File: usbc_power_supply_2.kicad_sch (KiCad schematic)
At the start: 22 parts, among them J1 USB4125-GF-A-0190, J2 B2B-PH-K-SLFSN, J3 B2B-PH-K-SLFSN, Q1 DMG3415UFY4Q-7, U1 MBR0540T3G, U2 MCP73833-AMI/MF

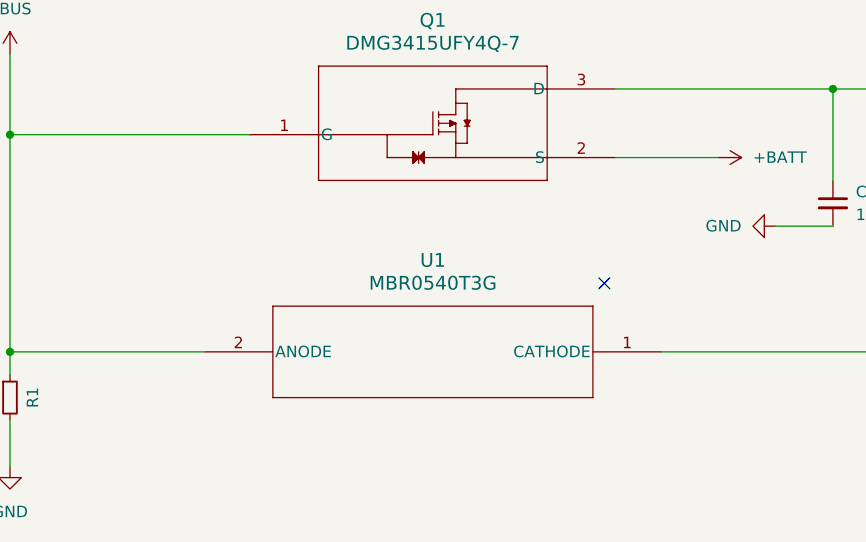
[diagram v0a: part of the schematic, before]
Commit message: updates mounting holes with pads, optional 1A shottkyx
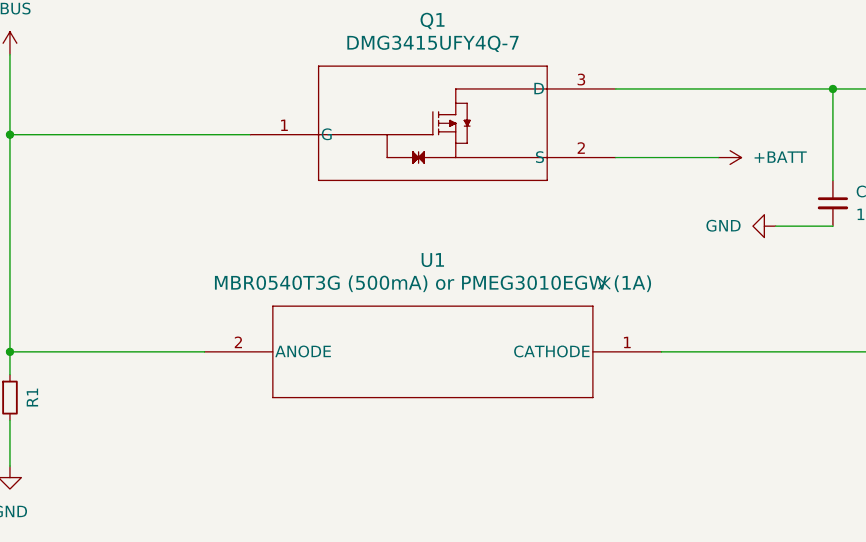
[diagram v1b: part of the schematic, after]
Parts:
- H1, H2: footprint MountingHole:MountingHole_2.2mm_M2 -> MountingHole:MountingHole_2.2mm_M2_Pad
- U1: value MBR0540T3G -> MBR0540T3G (500mA) or PMEG3010EGW (1A)
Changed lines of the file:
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@@
       (effects (font (size 1.524 1.524)))
     )
-    (property "Value" "MBR0540T3G" (at 78.74 133.35 0)
+    (property "Value" "MBR0540T3G (500mA) or  PMEG3010EGW  (1A)" (at 78.74 133.35 0)
       (effects (font (size 1.524 1.524)))
     )
@@
       (effects (font (size 1.27 1.27)) (justify left))
     )
-    (property "Footprint" "MountingHole:MountingHole_2.2mm_M2" (at 255.27 138.43 0)
+    (property "Footprint" "MountingHole:MountingHole_2.2mm_M2_Pad" (at 255.27 138.43 0)
       (effects (font (size 1.27 1.27)) hide)
     )
@@
       (effects (font (size 1.27 1.27)) (justify left))
     )
-    (property "Footprint" "MountingHole:MountingHole_2.2mm_M2" (at 255.27 128.27 0)
-      (effects (font (size 1.27 1.27)) hide)
-    )
+    (property "Footprint" "MountingHole:MountingHole_2.2mm_M2_Pad" (at 255.27 128.27 0)
+      (effects (font (size 1.27 1.27)) hide)
+    )
